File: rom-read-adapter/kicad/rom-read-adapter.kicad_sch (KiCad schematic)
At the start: 51 parts, among them J1 Host_Conn_02x25, J10 Conn_01x04_Pin, J2 ZIF-48, J3 Conn_01x24_Pin, J4 Conn_01x13_Pin, J5 Conn_01x05_Pin

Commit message: WIP rom-read-adapter sch: Added J6.
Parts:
- added J6: Conn_01x05_Pin, symbol Connector:Conn_01x05_Pin
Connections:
- net D3: now also J6.1 (D3)
- net D4: now also J6.2 (D4)
- net D5: now also J6.3 (D5)
- net D6: now also J6.4 (D6)
- net D7: now also J6.5 (D7)
- net at J2., J2.28: now also J5.28 (Pin_4); no longer J5.2 (Pin_2)
- net at J2.25: now also J5.25 (Pin_1); no longer J5.5 (Pin_5)
- net at J2.26: now also J5.26 (Pin_2); no longer J5.4 (Pin_4)
- net at J2.27: now also J5.27 (Pin_3); no longer J5.3 (Pin_3)
- net at J2.29: now also J5.29 (Pin_5); no longer J5.1 (Pin_1)
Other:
- moved on the sheet: J4, J5
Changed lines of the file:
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@@
 	(global_label "A7"
 		(shape output)
-		(at 113.03 95.25 180)
+		(at 115.57 95.25 180)
 		(fields_autoplaced yes)
 		(effects
@@
 		)
 		(property "Intersheetrefs" "${INTERSHEET_REFS}"
-			(at 107.7467 95.25 0)
+			(at 110.2867 95.25 0)
 			(effects
 				(font
@@
 	(global_label "A2"
 		(shape output)
-		(at 113.03 107.95 180)
+		(at 115.57 107.95 180)
 		(fields_autoplaced yes)
 		(effects
@@
 		)
 		(property "Intersheetrefs" "${INTERSHEET_REFS}"
-			(at 107.7467 107.95 0)
+			(at 110.2867 107.95 0)
 			(effects
 				(font
@@
 	(global_label "D3"
 		(shape input)
-		(at 171.45 139.7 0)
+		(at 161.29 123.19 0)
 		(fields_autoplaced yes)
 		(effects
@@
 		)
 		(property "Intersheetrefs" "${INTERSHEET_REFS}"
-			(at 176.9147 139.7 0)
+			(at 166.7547 123.19 0)
 			(effects
 				(font
@@
 	(global_label "A12"
 		(shape output)
-		(at 113.03 92.71 180)
+		(at 115.57 92.71 180)
 		(fields_autoplaced yes)
 		(effects
@@
 		)
 		(property "Intersheetrefs" "${INTERSHEET_REFS}"
-			(at 106.5372 92.71 0)
+			(at 109.0772 92.71 0)
 			(effects
 				(font
@@
 	(global_label "D2"
 		(shape input)
-		(at 113.03 120.65 180)
+		(at 115.57 120.65 180)
 		(fields_autoplaced yes)
 		(effects
@@
 		)
 		(property "Intersheetrefs" "${INTERSHEET_REFS}"
-			(at 107.5653 120.65 0)
+			(at 110.1053 120.65 0)
 			(effects
 				(font
@@
 	(global_label "D1"
 		(shape input)
-		(at 113.03 118.11 180)
+		(at 115.57 118.11 180)
 		(fields_autoplaced yes)
 		(effects
@@
 		)
 		(property "Intersheetrefs" "${INTERSHEET_REFS}"
-			(at 107.5653 118.11 0)
+			(at 110.1053 118.11 0)
 			(effects
 				(font
@@
 	(global_label "A0"
 		(shape output)
-		(at 113.03 113.03 180)
+		(at 115.57 113.03 180)
 		(fields_autoplaced yes)
 		(effects
@@
 		)
 		(property "Intersheetrefs" "${INTERSHEET_REFS}"
-			(at 107.7467 113.03 0)
+			(at 110.2867 113.03 0)
 			(effects
 				(font
@@
 	(global_label "A5"
 		(shape output)
-		(at 113.03 100.33 180)
+		(at 115.57 100.33 180)
 		(fields_autoplaced yes)
 		(effects
@@
 		)
 		(property "Intersheetrefs" "${INTERSHEET_REFS}"
-			(at 107.7467 100.33 0)
+			(at 110.2867 100.33 0)
 			(effects
 				(font
@@
 	(global_label "D4"
 		(shape input)
-		(at 171.45 137.16 0)
+		(at 161.29 120.65 0)
 		(fields_autoplaced yes)
 		(effects
@@
 		)
 		(property "Intersheetrefs" "${INTERSHEET_REFS}"
-			(at 176.9147 137.16 0)
+			(at 166.7547 120.65 0)
 			(effects
 				(font
@@
 	(global_label "A1"
 		(shape output)
-		(at 113.03 110.49 180)
+		(at 115.57 110.49 180)
 		(fields_autoplaced yes)
 		(effects
@@
 		)
 		(property "Intersheetrefs" "${INTERSHEET_REFS}"
-			(at 107.7467 110.49 0)
+			(at 110.2867 110.49 0)
 			(effects
 				(font
@@
 	(global_label "A3"
 		(shape output)
-		(at 113.03 105.41 180)
+		(at 115.57 105.41 180)
 		(fields_autoplaced yes)
 		(effects
@@
 		)
 		(property "Intersheetrefs" "${INTERSHEET_REFS}"
-			(at 107.7467 105.41 0)
+			(at 110.2867 105.41 0)
 			(effects
 				(font
@@
 	(global_label "D5"
 		(shape input)
-		(at 171.45 134.62 0)
+		(at 161.29 118.11 0)
 		(fields_autoplaced yes)
 		(effects
@@
 		)
 		(property "Intersheetrefs" "${INTERSHEET_REFS}"
-			(at 176.9147 134.62 0)
+			(at 166.7547 118.11 0)
 			(effects
 				(font
@@
 	(global_label "A6"
 		(shape output)
-		(at 113.03 97.79 180)
+		(at 115.57 97.79 180)
 		(fields_autoplaced yes)
 		(effects
@@
 		)
 		(property "Intersheetrefs" "${INTERSHEET_REFS}"
-			(at 107.7467 97.79 0)
+			(at 110.2867 97.79 0)
 			(effects
 				(font
@@
 	(global_label "D6"
 		(shape input)
-		(at 171.45 132.08 0)
+		(at 161.29 115.57 0)
 		(fields_autoplaced yes)
 		(effects
@@
 		)
 		(property "Intersheetrefs" "${INTERSHEET_REFS}"
-			(at 176.9147 132.08 0)
+			(at 166.7547 115.57 0)
 			(effects
 				(font
@@
 	(global_label "D7"
 		(shape input)
-		(at 171.45 129.54 0)
+		(at 161.29 113.03 0)
 		(fields_autoplaced yes)
 		(effects
@@
 		)
 		(property "Intersheetrefs" "${INTERSHEET_REFS}"
-			(at 176.9147 129.54 0)
+			(at 166.7547 113.03 0)
 			(effects
 				(font
@@
 	(global_label "A4"
 		(shape output)
-		(at 113.03 102.87 180)
+		(at 115.57 102.87 180)
 		(fields_autoplaced yes)
 		(effects
@@
 		)
 		(property "Intersheetrefs" "${INTERSHEET_REFS}"
-			(at 107.7467 102.87 0)
+			(at 110.2867 102.87 0)
 			(effects
 				(font
@@
 	(global_label "D0"
 		(shape input)
-		(at 113.03 115.57 180)
+		(at 115.57 115.57 180)
 		(fields_autoplaced yes)
 		(effects
@@
 		)
 		(property "Intersheetrefs" "${INTERSHEET_REFS}"
-			(at 107.5653 115.57 0)
+			(at 110.1053 115.57 0)
 			(effects
 				(font
@@
 	(symbol
 		(lib_id "power:GND")
-		(at 113.03 123.19 0)
+		(at 115.57 123.19 0)
 		(unit 1)
 		(exclude_from_sim no)
@@
 		(fields_autoplaced yes)
 		(property "Reference" "#PWR03"
-			(at 113.03 129.54 0)
+			(at 115.57 129.54 0)
 			(effects
 				(font
@@
 		)
 		(property "Value" "GND"
-			(at 113.03 128.27 0)
+			(at 115.57 128.27 0)
 			(effects
 				(font
@@
 		)
 		(property "Footprint" ""
-			(at 113.03 123.19 0)
+			(at 115.57 123.19 0)
 			(effects
 				(font
@@
 		)
 		(property "Datasheet" ""
-			(at 113.03 123.19 0)
+			(at 115.57 123.19 0)
 			(effects
 				(font
@@
 		)
 		(property "Description" "Power symbol creates a global label with name \"GND\" , ground"
-			(at 113.03 123.19 0)
+			(at 115.57 123.19 0)
 			(effects
 				(font
@@
 	)
 	(symbol
+		(lib_name "Conn_01x05_Pin_1")
 		(lib_id "Connector:Conn_01x05_Pin")
-		(at 153.67 118.11 0)
-		(mirror y)
+		(at 153.67 118.11 180)
 		(unit 1)
 		(exclude_from_sim no)
@@
 		(dnp no)
 		(property "Reference" "J5"
-			(at 153.67 125.222 0)
+			(at 153.1231 125.1429 0)
 			(effects
 				(font
@@
 		)
 		(property "Value" "Conn_01x05_Pin"
-			(at 153.035 110.49 0)
+			(at 153.035 125.73 0)
 			(effects
 				(font
@@
 			)
 		)
-		(pin "5"
+		(pin "27"
 		)
-		(pin "2"
+		(pin "29"
 		)
-		(pin "1"
+		(pin "25"
 		)
-		(pin "3"
+		(pin "26"
 		)
-		(pin "4"
+		(pin "28"
 		)
 		(instances
@@
 	(symbol
 		(lib_id "Connector:Conn_01x13_Pin")
-		(at 118.11 107.95 0)
+		(at 120.65 107.95 0)
 		(mirror y)
 		(unit 1)
@@
 		(dnp no)
 		(property "Reference" "J4"
-			(at 116.586 125.222 0)
+			(at 119.126 125.222 0)
 			(effects
 				(font
@@
 		)
 		(property "Value" "Conn_01x13_Pin"
-			(at 119.38 109.2199 0)
+			(at 121.92 109.2199 0)
 			(effects
 				(font
@@
 		)
 		(property "Footprint" ""
-			(at 118.11 107.95 0)
+			(at 120.65 107.95 0)
 			(effects
 				(font
@@
 		)
 		(property "Datasheet" "~"
-			(at 118.11 107.95 0)
+			(at 120.65 107.95 0)
 			(effects
 				(font
@@
 		)
 		(property "Description" "Generic connector, single row, 01x13, script generated"
-			(at 122.174 88.138 0)
+			(at 124.714 88.138 0)
 			(effects
 				(font
@@
 		(dnp no)
 		(property "Reference" "J3"
-			(at 123.19 125.222 0)
+			(at 123.952 125.222 0)
 			(effects
 				(font
@@
 					(unit 1)
 				)
+			)
+		)
+	)
+	(symbol
+		(lib_id "Connector:Conn_01x05_Pin")
+		(at 156.21 118.11 0)
+		(mirror x)
+		(unit 1)
+		(exclude_from_sim no)
+		(in_bom yes)
+		(on_board yes)
+		(dnp no)
+		(property "Reference" "J6"
+			(at 157.226 125.222 0)
+			(effects
+				(font
+					(size 1.27 1.27)
+				)
+			)
+		)
+		(property "Value" "Conn_01x05_Pin"
+			(at 156.845 125.73 0)
+			(effects
+				(font
+					(size 1.27 1.27)
+				)
+				(hide yes)
+			)
+		)
+		(property "Footprint" ""
+			(at 156.21 118.11 0)
+			(effects
+				(font
+					(size 1.27 1.27)
+				)
+				(hide yes)
+			)
+		)
+		(property "Datasheet" "~"
+			(at 156.21 118.11 0)
+			(effects
+				(font
+					(size 1.27 1.27)
+				)
+				(hide yes)
+			)
+		)
+		(property "Description" "Generic connector, single row, 01x05, script generated"
+			(at 157.988 106.68 0)
+			(effects
+				(font
+					(size 1.27 1.27)
+				)
+				(hide yes)
+			)
+		)
+		(pin "3"
+		)
+		(pin "5"
+		)
+		(pin "2"
+		)
+		(pin "4"
+		)
+		(pin "1"
+		)
+		(instances
+			(project ""
+				(path "/65bf6d13-0c24-4e8f-8a57-e3ae2776eac6"
+					(reference "J6")
+					(unit 1)
+				)

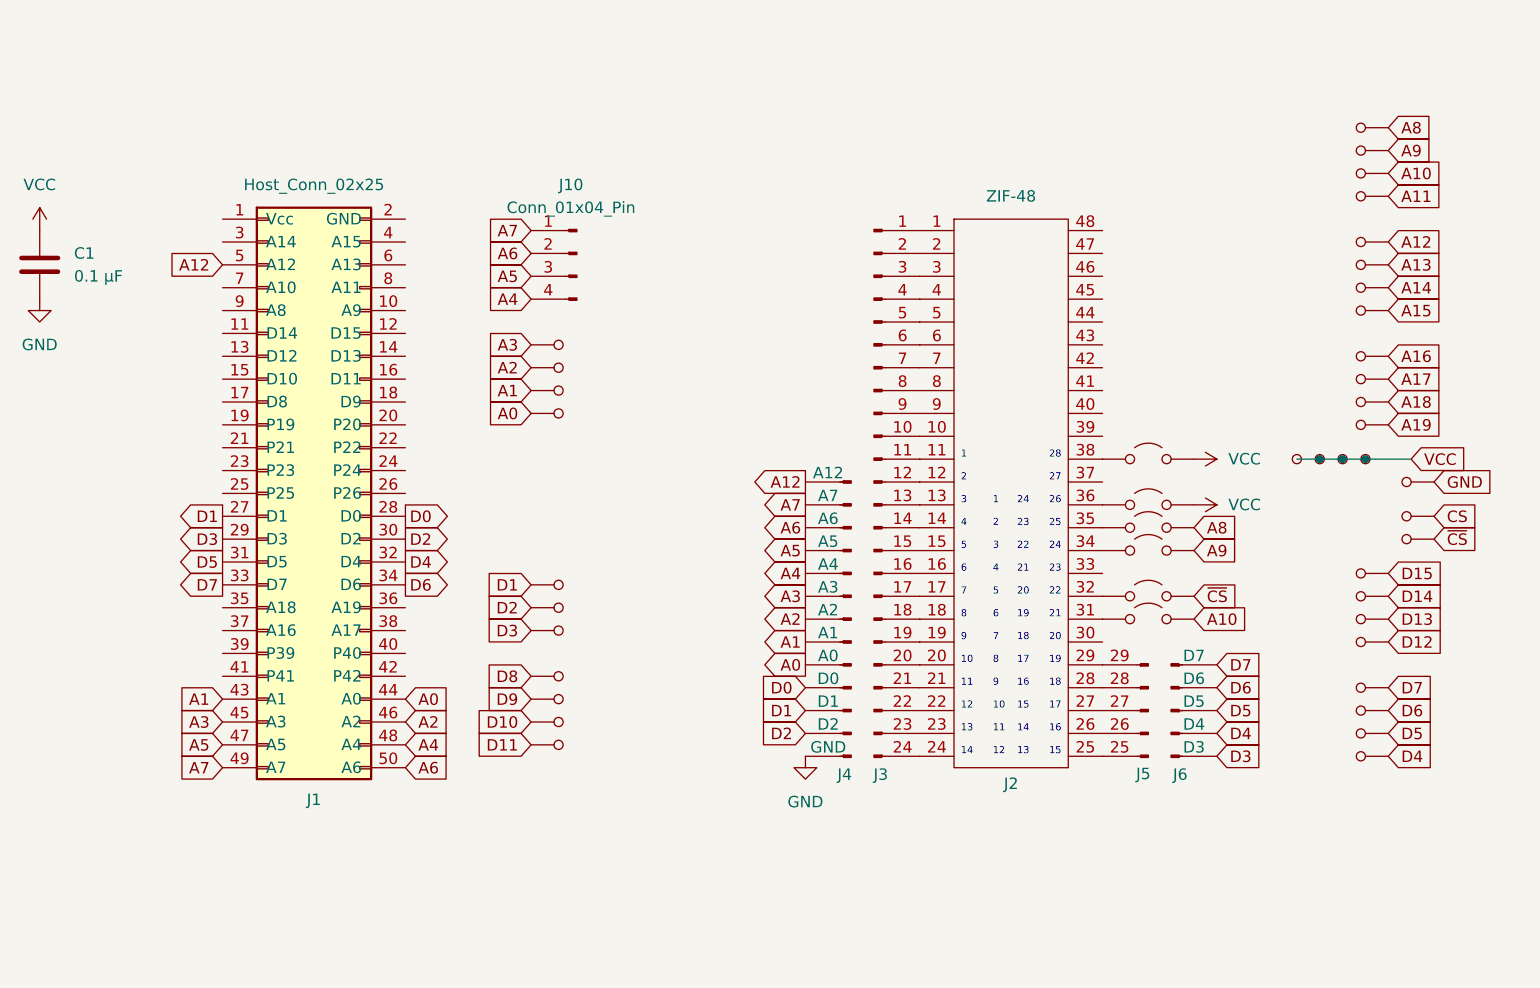
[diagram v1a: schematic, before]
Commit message: WIP rom-read-adapter sch: Added remaining data and address pins / nets on host connector
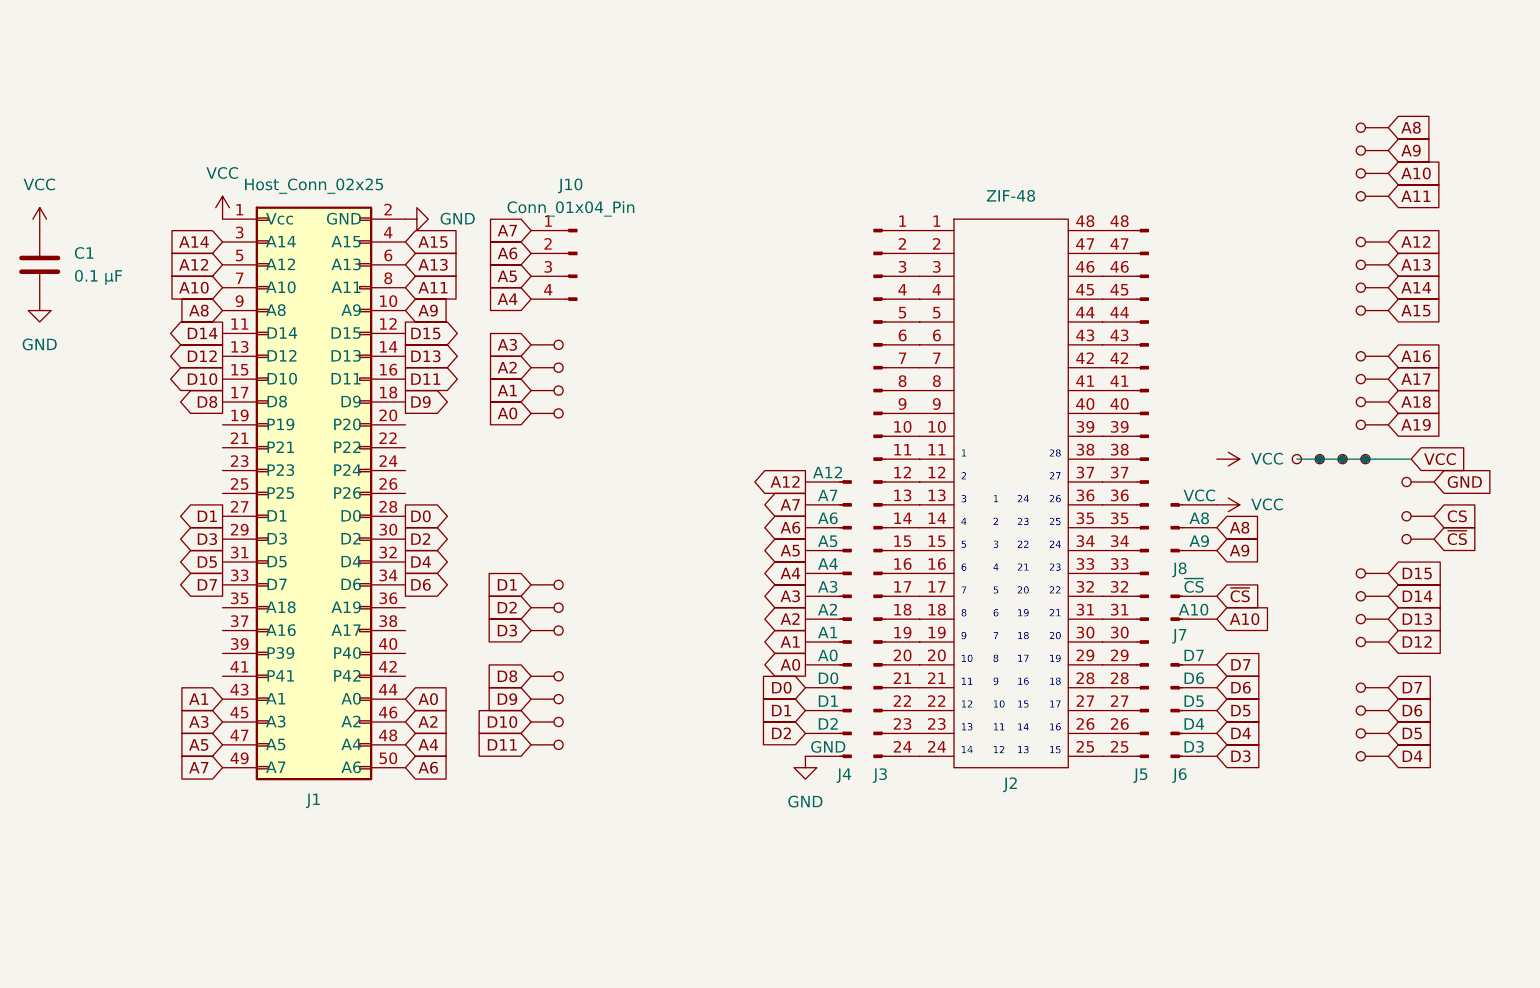
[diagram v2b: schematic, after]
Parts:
- removed J5: Conn_01x05_Pin, symbol Connector:Conn_01x05_Pin
- removed JP31, JP32, JP34, JP35, JP36, JP38: Jumper_2_Open, symbol Jumper:Jumper_2_Open
- added J5: Conn_01x24_Pin, symbol Connector:Conn_01x24_Pin
- added J7: Conn_01x02_Pin, symbol Connector:Conn_01x02_Pin
- added J8: Conn_01x03_Pin, symbol Connector:Conn_01x03_Pin
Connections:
- net A10: now also J1.7 (A10), J7.1 (A10)
- net A11: now also J1.8 (A11)
- net A13: now also J1.6 (A13)
- net A14: now also J1.3 (A14)
- net A15: now also J1.4 (A15)
- net A8: now also J1.9 (A8), J8.2 (A8)
- net A9: now also J1.10 (A9), J8.1 (A9)
- net D10: now also J1.15 (D10)
- net D11: now also J1.16 (D11)
- net D12: now also J1.13 (D12)
- net D13: now also J1.14 (D13)
- net D14: now also J1.11 (D14)
- net D15: now also J1.12 (D15)
- net D8: now also J1.17 (D8)
- net D9: now also J1.18 (D9)
- net GND: now also J1.2 (GND)
- net VCC: now also J1.1 (Vcc), J8.3 (VCC)
- net ~{CS}: now also J7.2 (~{CS})
- net at J2., J2.28: now also J5.28 (Pin_4)
- net at J2.25: now also J5.25 (Pin_1)
- net at J2.26: now also J5.26 (Pin_2)
- net at J2.27: now also J5.27 (Pin_3)
- net at J2.29: now also J5.29 (Pin_5)
- net at J2.30: now also J5.30 (Pin_6)
- net at J2.31: now also J5.31 (Pin_7)
- net at J2.32: now also J5.32 (Pin_8)
- net at J2.33: now also J5.33 (Pin_9)
- net at J2.34: now also J5.34 (Pin_10)
- net at J2.35: now also J5.35 (Pin_11)
- net at J2.36: now also J5.36 (Pin_12)
- net at J2.37: now also J5.37 (Pin_13)
- net at J2.38: now also J5.38 (Pin_14)
- net at J2.39: now also J5.39 (Pin_15)
- net at J2.40: now also J5.40 (Pin_16)
- net at J2.41: now also J5.41 (Pin_17)
- net at J2.42: now also J5.42 (Pin_18)
- net at J2.43: now also J5.43 (Pin_19)
- net at J2.44: now also J5.44 (Pin_20)
- net at J2.45: now also J5.45 (Pin_21)
- net at J2.46: now also J5.46 (Pin_22)
- net at J2.47: now also J5.47 (Pin_23)
- net at J2.48: now also J5.48 (Pin_24)

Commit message: WIP rom-read-adapter sch: Completed Schematic
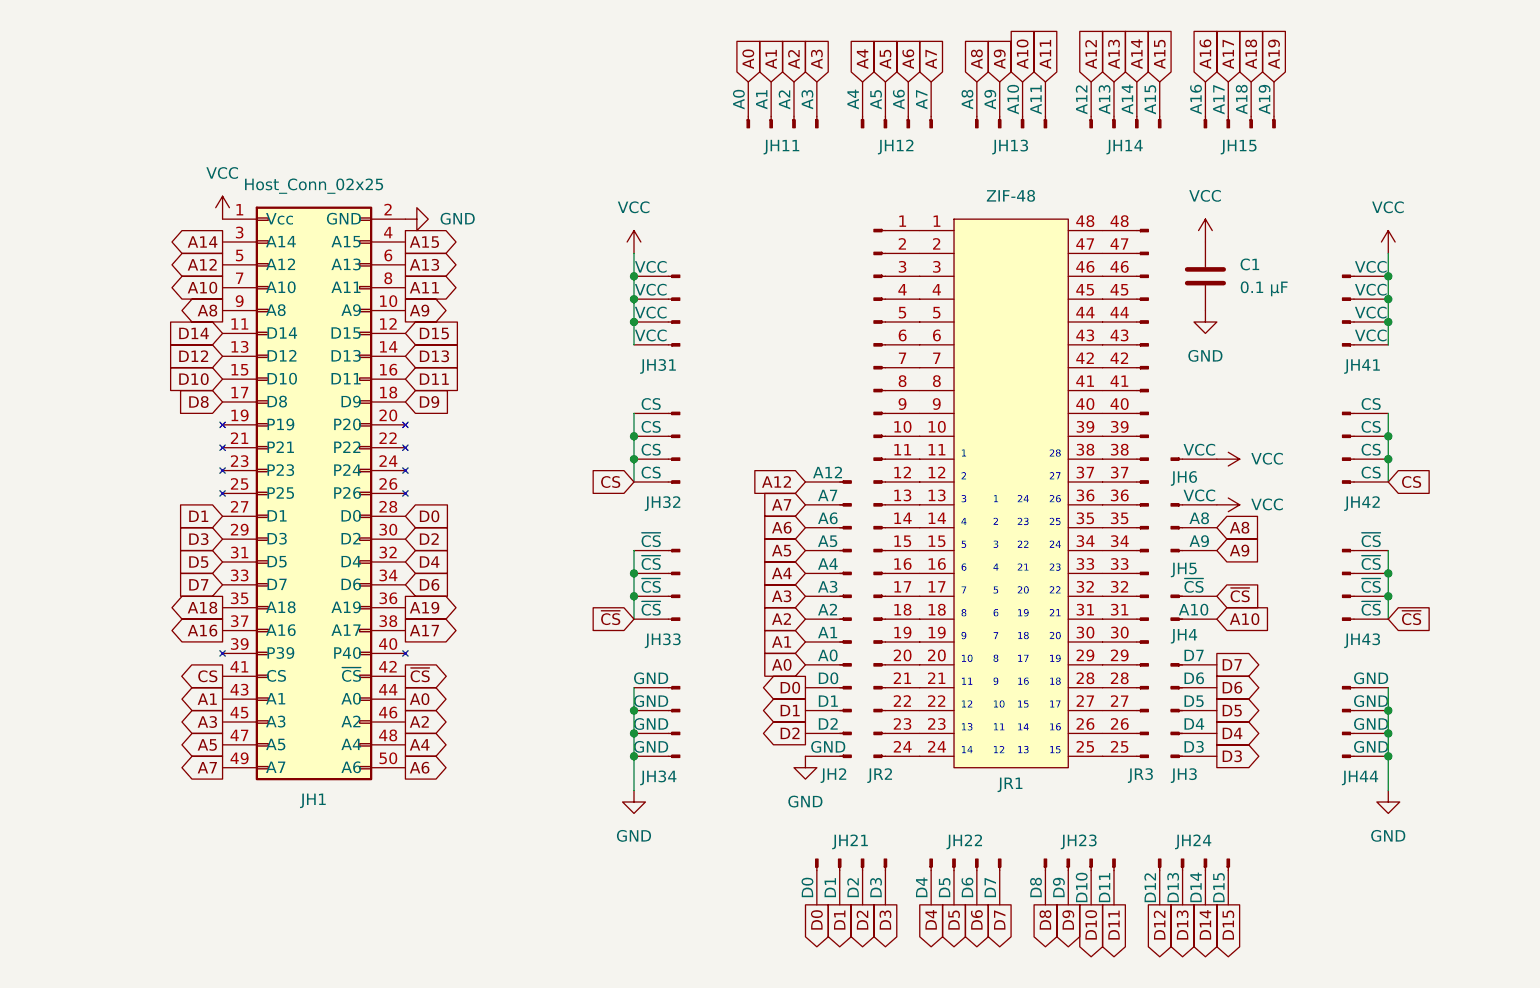
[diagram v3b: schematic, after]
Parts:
- removed J10: Conn_01x04_Pin, symbol Connector:Conn_01x04_Pin
- removed JPA1, JPA10, JPA11, JPA12, JPA13, JPA14, JPA15, JPA16, JPA17, JPA18, JPA19, JPA2, JPA20, JPA25, JPA26, JPA27, JPA28, JPA29, JPA3, JPA30, JPA31, JPA32, JPA34, JPA35, JPA36, JPA37, JPA38, JPA39, JPA4, JPA40, JPA41, JPA42, JPA43, JPA5, JPA6, JPA7, JPA8, JPA9: Header_Pin, symbol 0cjs-hwdev:Header_Pin
- added JH11, JH12, JH13, JH14, JH15, JH21, JH22, JH23, JH24, JH31, JH32, JH33, JH34, JH41, JH42, JH43, JH44: Conn_01x04_Pin, symbol Connector:Conn_01x04_Pin
- added JH6: Conn_01x01_Pin, symbol Connector:Conn_01x01_Pin
- renumbered J1 to JH1, J4 to JH2, J6 to JH3, J7 to JH4, J8 to JH5, J2 to JR1, J3 to JR2, J5 to JR3
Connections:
- net A0: now also JH11.1 (A0)
- net A1: now also JH11.2 (A1)
- net A10: now also JH13.3 (A10)
- net A11: now also JH13.4 (A11)
- net A12: now also JH14.1 (A12)
- net A13: now also JH14.2 (A13)
- net A14: now also JH14.3 (A14)
- net A15: now also JH14.4 (A15)
- net A16: now also JH1.37 (A16), JH15.1 (A16)
- net A17: now also JH1.38 (A17), JH15.2 (A17)
- net A18: now also JH1.35 (A18), JH15.3 (A18)
- net A19: now also JH1.36 (A19), JH15.4 (A19)
- net A2: now also JH11.3 (A2)
- net A3: now also JH11.4 (A3)
- net A4: now also JH12.1 (A4)
- net A5: now also JH12.2 (A5)
- net A6: now also JH12.3 (A6)
- net A7: now also JH12.4 (A7)
- net A8: now also JH13.1 (A8)
- net A9: now also JH13.2 (A9)
- net CS: now also JH1.41 (CS), JH32.1 (CS), JH32.2 (CS), JH32.3 (CS), JH32.4 (CS), JH42.1 (CS), JH42.2 (CS), JH42.3 (CS), JH42.4 (CS)
- net D0: now also JH21.1 (D0)
- net D1: now also JH21.2 (D1)
- net D10: now also JH23.3 (D10)
- net D11: now also JH23.4 (D11)
- net D12: now also JH24.1 (D12)
- net D13: now also JH24.2 (D13)
- net D14: now also JH24.3 (D14)
- net D15: now also JH24.4 (D15)
- net D2: now also JH21.3 (D2)
- net D3: now also JH21.4 (D3)
- net D4: now also JH22.1 (D4)
- net D5: now also JH22.2 (D5)
- net D6: now also JH22.3 (D6)
- net D7: now also JH22.4 (D7)
- net D8: now also JH23.1 (D8)
- net D9: now also JH23.2 (D9)
- net GND: now also JH34.1 (GND), JH34.2 (GND), JH34.3 (GND), JH34.4 (GND), JH44.1 (GND), JH44.2 (GND), JH44.3 (GND), JH44.4 (GND)
- net VCC: now also JH31.1 (VCC), JH31.2 (VCC), JH31.3 (VCC), JH31.4 (VCC), JH41.1 (VCC), JH41.2 (VCC), JH41.3 (VCC), JH41.4 (VCC), JH6.1 (VCC)
- net ~{CS}: now also JH1.42 (~{CS}), JH33.1 (~{CS}), JH33.2 (~{CS}), JH33.3 (~{CS}), JH33.4 (~{CS}), JH43.1 (~{CS}), JH43.2 (~{CS}), JH43.3 (~{CS}), JH43.4 (~{CS})
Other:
- moved on the sheet: C1
